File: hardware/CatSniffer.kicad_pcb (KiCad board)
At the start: 4 copper layers, 81 x 20 mm, 86 parts, among them J1 Antenna, J2 Conn_01x06_Female, J3 Conn_01x06_Female, P1 USB_C_Plug_USB2.0, SW1 SW, U1 AP2112K-3.3, U2 RFSW8006QTR7, U3 ATSAMD21E18A, U4 0900PC15A0036, U5 0900FM15D0039, U6 SW409, U7 SX1262IMLTRT, U8 CC1352R1F3RGZR, Y1 48MHz, Y2 32.768kHz, Y3 32Mhz

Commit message: ChngCC1352P
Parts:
- U8: value CC1352R1F3RGZR -> CC1352P1F3RGZT
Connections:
- U8 pad 5: /RX_TX -> Net-(U8-Pad5)
- U8 pad 6: Net-(C34-Pad1) -> Net-(U8-Pad6)
- U8 pad 7: Net-(C36-Pad1) -> /RX_TX
- U8 pad 8: Net-(U8-Pad8) -> Net-(C34-Pad1)
- U8 pad 9: Net-(U8-Pad9) -> Net-(C36-Pad1)
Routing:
- net Net-(C36-Pad1): track 4.32 -> 3.40 mm
- net /RX_TX: track 6.78 -> 7.66 mm
- net Net-(C34-Pad1): track 6.01 -> 5.45 mm

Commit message: UpdateKicad6
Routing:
- added copper zone on In2.Cu, net +3V3
- added copper zone on In2.Cu, net /VDDR
- added copper zone on In2.Cu, net /VDDS
- added copper zone on In1.Cu, net GND
- removed copper zone on VCC, net +3V3
- removed copper zone on VCC, net /VDDR
- removed copper zone on VCC, net /VDDS
- removed copper zone on GND, net GND
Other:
- net class Default removed

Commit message: update version
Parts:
- removed C28, C30: 47pF, Capacitor_SMD:C_0603_1608Metric
- U6: value SW409 -> PE42421; footprint CatSniffer:SW409 -> Package_TO_SOT_SMD:SOT-363_SC-70-6
- moved R8 0.59 mm to (139.1, 105.1)
- moved R7 0.38 mm to (139.0, 100.8)
- moved U6 0.20 mm to (138.9, 103.0), turned to 0 degrees
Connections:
- J2 pad 6: Net-(J2-Pad6) -> unconnected-(J2-Pad6)
- J3 pad 6: Net-(J3-Pad6) -> unconnected-(J3-Pad6)
- U1 pad 4: Net-(U1-Pad4) -> unconnected-(U1-Pad4)
- U6 pad 1: Net-(C28-Pad2) -> /SW_RFO
- U6 pad 3: Net-(C30-Pad2) -> /SW_RFI
- U8 pad 10: Net-(U8-Pad10) -> unconnected-(U8-Pad10)
- U8 pad 11: Net-(U8-Pad11) -> unconnected-(U8-Pad11)
- U8 pad 12: Net-(U8-Pad12) -> unconnected-(U8-Pad12)
- U8 pad 14: Net-(U8-Pad14) -> unconnected-(U8-Pad14)
- U8 pad 15: Net-(U8-Pad15) -> unconnected-(U8-Pad15)
- U8 pad 16: Net-(U8-Pad16) -> unconnected-(U8-Pad16)
- U8 pad 17: Net-(U8-Pad17) -> unconnected-(U8-Pad17)
- U8 pad 20: Net-(U8-Pad20) -> unconnected-(U8-Pad20)
- U8 pad 26: Net-(U8-Pad26) -> unconnected-(U8-Pad26)
- U8 pad 27: Net-(U8-Pad27) -> unconnected-(U8-Pad27)
- U8 pad 28: Net-(U8-Pad28) -> unconnected-(U8-Pad28)
- U8 pad 29: Net-(U8-Pad29) -> unconnected-(U8-Pad29)
- U8 pad 30: Net-(U8-Pad30) -> unconnected-(U8-Pad30)
- U8 pad 31: Net-(U8-Pad31) -> unconnected-(U8-Pad31)
- U8 pad 32: Net-(U8-Pad32) -> unconnected-(U8-Pad32)
- U8 pad 36: Net-(U8-Pad36) -> unconnected-(U8-Pad36)
- U8 pad 38: Net-(U8-Pad38) -> unconnected-(U8-Pad38)
- U8 pad 39: Net-(U8-Pad39) -> unconnected-(U8-Pad39)
- U8 pad 40: Net-(U8-Pad40) -> unconnected-(U8-Pad40)
- U8 pad 41: Net-(U8-Pad41) -> unconnected-(U8-Pad41)
- U8 pad 42: Net-(U8-Pad42) -> unconnected-(U8-Pad42)
- U8 pad 43: Net-(U8-Pad43) -> unconnected-(U8-Pad43)
- U8 pad 5: Net-(U8-Pad5) -> unconnected-(U8-Pad5)
- U8 pad 6: Net-(U8-Pad6) -> unconnected-(U8-Pad6)
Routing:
- net GND: track 309.6 -> 318.9 mm
- net /SW_RFI: track 2.87 -> 6.34 mm
- net /SW_RFO: track 3.97 -> 7.32 mm
- net Net-(C28-Pad2): track 2.47 -> 0.00 mm
- net Net-(C30-Pad2): track 2.45 -> 0.00 mm
- net Net-(C35-Pad1): track 4.70 -> 3.54 mm
- net /ANT_SW: track 36.8 -> 37.6 mm
- net Net-(C31-Pad1): track 2.77 -> 3.48 mm
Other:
- board text added: "CatSniffer V2.0"
- board text removed: "CatSniffer V1.2"

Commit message: Update label 2.0
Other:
- board text added: "CatSniffer v2.0"
- board text removed: "CatSniffer v1.2"
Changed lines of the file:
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@@
     (43 "Eco2.User" user "User.Eco2")
     (44 "Edge.Cuts" user)
-    (45 "Margin" user)
+    (45 "Margin" user "Margen")
     (46 "B.CrtYd" user "B.Courtyard")
     (47 "F.CrtYd" user "F.Courtyard")
@@
   (gr_line (start 90 120) (end 161 120) (layer "Edge.Cuts") (width 0.15))
   (gr_line (start 85 105) (end 85 115) (layer "Edge.Cuts") (width 0.15))
-  (gr_text "CatSniffer\nv1.2" (at 98.298 110.236) (layer "B.SilkS")
+  (gr_text "CatSniffer\nv2.0" (at 98.298 110.236) (layer "B.SilkS")
     (effects (font (size 1.5 1.5) (thickness 0.25)) (justify mirror))
   )

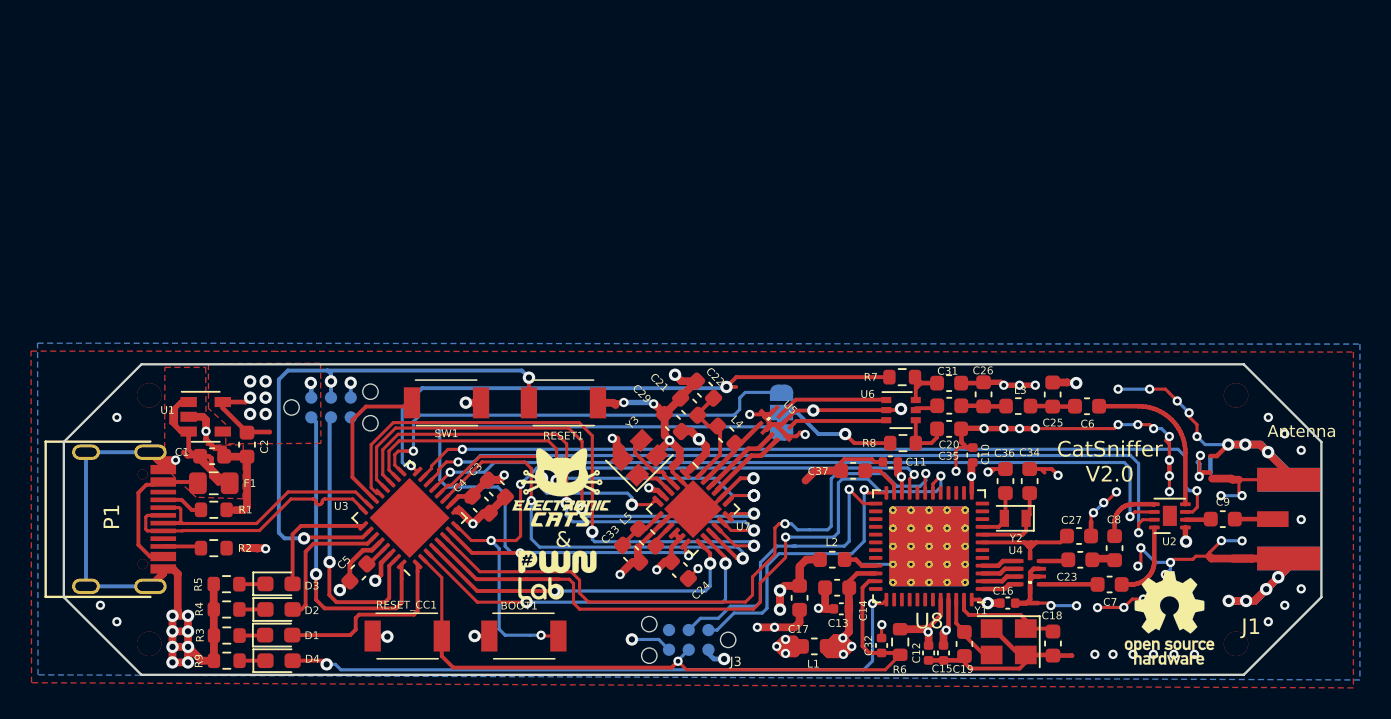
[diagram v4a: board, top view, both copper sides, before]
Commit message: change of components rp2040
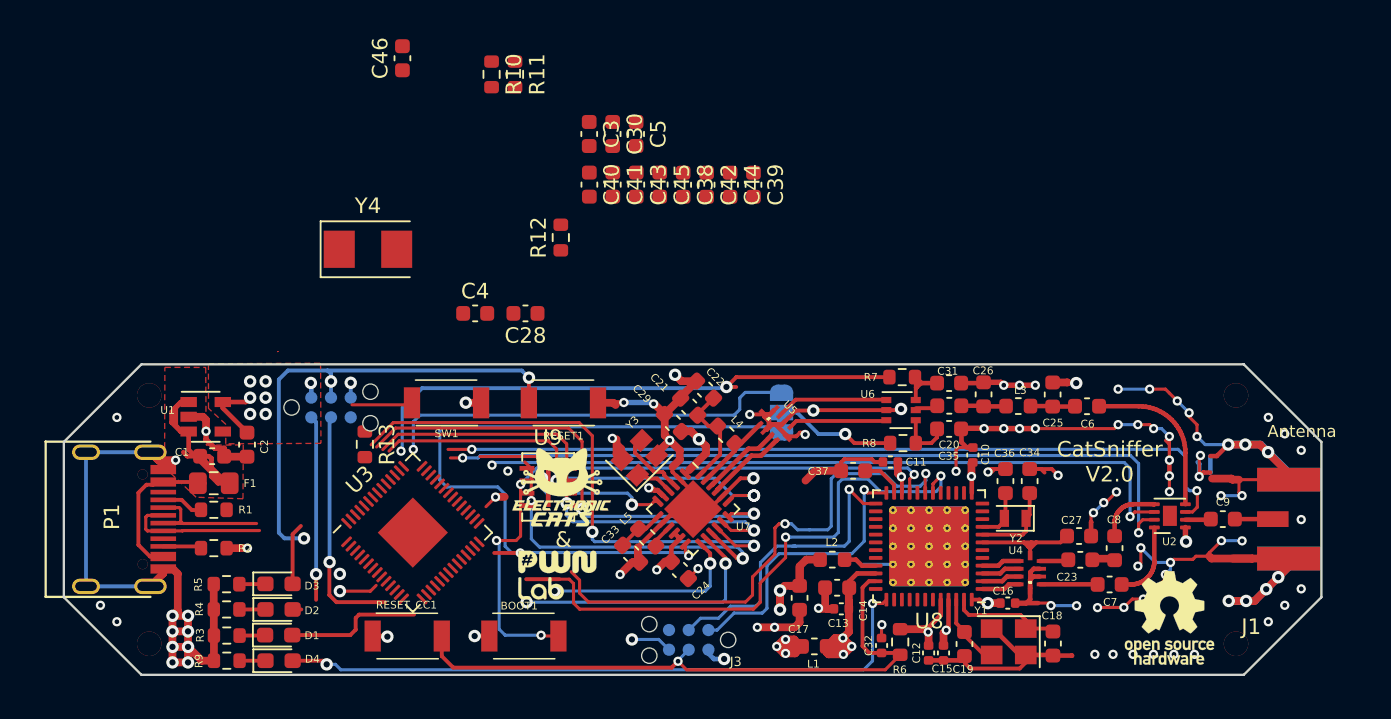
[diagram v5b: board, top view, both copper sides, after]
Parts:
- added C28: 27pF, Capacitor_SMD:C_0603_1608Metric, F.Cu at (114.7, 96.7)
- added C30: 0.1uF, Capacitor_SMD:C_0603_1608Metric, F.Cu at (120.3, 85.2)
- added C38: 1uF, Capacitor_SMD:C_0603_1608Metric, F.Cu at (124.9, 88.4)
- added C39: 0.1uF, Capacitor_SMD:C_0603_1608Metric, F.Cu at (129.4, 88.4)
- added C40: 0.1uF, Capacitor_SMD:C_0603_1608Metric, F.Cu at (118.8, 88.4)
- added C41: 0.1uF, Capacitor_SMD:C_0603_1608Metric, F.Cu at (120.4, 88.4)
- added C42: 0.1uF, Capacitor_SMD:C_0603_1608Metric, F.Cu at (126.4, 88.4)
- added C43: 0.1uF, Capacitor_SMD:C_0603_1608Metric, F.Cu at (121.9, 88.4)
- added C44: 0.1uF, Capacitor_SMD:C_0603_1608Metric, F.Cu at (127.9, 88.4)
- added C45: 0.1uF, Capacitor_SMD:C_0603_1608Metric, F.Cu at (123.4, 88.4)
- added C46: 0.1uF, Capacitor_SMD:C_0603_1608Metric, F.Cu at (106.8, 80.3)
- added R10: 27, Resistor_SMD:R_0603_1608Metric, F.Cu at (112.5, 81.3)
- added R11: 27, Resistor_SMD:R_0603_1608Metric, F.Cu at (114.1, 81.3)
- added R12: 1k, Resistor_SMD:R_0603_1608Metric, F.Cu at (117.0, 91.8)
- added R13: 10k, Resistor_SMD:R_0603_1608Metric, F.Cu at (104.4, 105.2)
- added U9: W25Q16JV, CatSniffer:W25Q16JVUUIQ, F.Cu at (116.2, 107.9)
- added Y4: 12MHz, Crystal:Crystal_SMD_5032-2Pin_5.0x3.2mm, F.Cu at (104.6, 92.6)
- C3: value 0.1uF -> 1uF
- C4: value 0.1uF -> 27pF
- U3: value ATSAMD21E18A -> RP2040; footprint Package_DFN_QFN:QFN-32-1EP_5x5mm_P0.5mm_EP3.65x3.65mm -> Package_DFN_QFN:QFN-56-1EP_7x7mm_P0.4mm_EP3.2x3.2mm
- moved C5 33.4 mm to (121.9, 85.2), turned to -90 degrees
- moved C3 23.6 mm to (118.8, 85.2), turned to -90 degrees
- moved C4 12.3 mm to (111.5, 96.7), turned to 0 degrees
- moved U3 0.97 mm to (107.5, 110.8), turned to 45 degrees
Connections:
- C3 pad 1: +3V3 -> +1V2
- C32 pad 1: /RESET_CC -> /RTS
- C4 pad 1: GND -> Net-(C4-Pad1)
- C4 pad 2: +3V3 -> GND
- C5 pad 1: GND -> +1V2
- C5 pad 2: Net-(C5-Pad2) -> GND
- J3 pad 3: /RESET_CC -> /RTS
- R6 pad 1: /RESET_CC -> /RTS
- RESET_CC1 pad 2: /RESET_CC -> /RTS
- SW1 pad 1: /U_SWITCH -> /QSPI_SS
- U3 pad 1: /LED3 -> +3V3
- U3 pad 10: GND -> +3V3
- U3 pad 11: /RESET_SX -> /CIPO
- U3 pad 12: /DIO3 -> /NSS
- U3 pad 14: /CTF2 -> /JTAG/TCK
- U3 pad 15: /CTF1 -> /cJTAG_TMSC
- U3 pad 16: /ANT_SW -> /JTAG/TDI
- U3 pad 17: /DIO22 -> /JTAG/TDO
- U3 pad 18: /NSS -> /RTS
- U3 pad 19: /COPI -> GND
- U3 pad 2: /RESET_CC -> /TXD
- U3 pad 20: /SCK -> Net-(C4-Pad1)
- U3 pad 21: /CIPO -> Net-(R12-Pad2)
- U3 pad 22: /U_SWITCH -> +3V3
- U3 pad 23: /D- -> +1V2
- U3 pad 24: /D+ -> /SWCLK
- U3 pad 25: /LED1 -> /SWDIO
- U3 pad 27: /LED2 -> /LED1
- U3 pad 28: GND -> /LED2
- U3 pad 29: Net-(C5-Pad2) -> /CTF2
- U3 pad 3: /BUSY -> /RXD
- U3 pad 30: +3V3 -> /CTF1
- U3 pad 31: /SWCLK -> /ANT_SW
- U3 pad 32: /SWDIO -> /DIO22
- U3 pad 33: (no net) -> +3V3
- U3 pad 4: /DIO1 -> /BOOT
- U3 pad 5: /TXD -> /RTS
- U3 pad 6: /RXD -> /BUSY
- U3 pad 7: /DIO2 -> /DIO1
- U3 pad 8: /BOOT -> /SCK
- U3 pad 9: +3V3 -> /COPI
- U8 pad 26: unconnected-(U8-Pad26) -> /JTAG/TDI
- U8 pad 27: unconnected-(U8-Pad27) -> /JTAG/TDO
- U8 pad 35: /RESET_CC -> /RTS
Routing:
- net /RESET_CC: track 46.8 -> 0.00 mm, vias 1 -> 0
- net /RTS: track 0.00 -> 41.3 mm, vias 0 -> 1
- net GND: track 318.9 -> 304.9 mm, vias 100 -> 98
- net /U_SWITCH: track 10.4 -> 0.00 mm
- net /RXD: track 42.6 -> 33.6 mm
- net /DIO1: track 22.0 -> 13.1 mm
- net /LED2: track 9.21 -> 0.66 mm
- net /D-: track 17.6 -> 9.16 mm
- net /SWDIO: track 20.6 -> 12.3 mm
- net /D+: track 17.6 -> 9.33 mm
- net +3V3: track 29.8 -> 22.0 mm, vias 16 -> 15
- net /BUSY: track 24.9 -> 17.3 mm
- net /TXD: track 46.3 -> 39.7 mm
- net /RESET_SX: track 28.3 -> 22.2 mm
- net /QSPI_SS: track 0.00 -> 4.68 mm
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- removed copper zone on B.Cu, net GND
- removed copper zone on F.Cu, net GND
- removed copper zone on In1.Cu, net GND

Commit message: change to rp2040
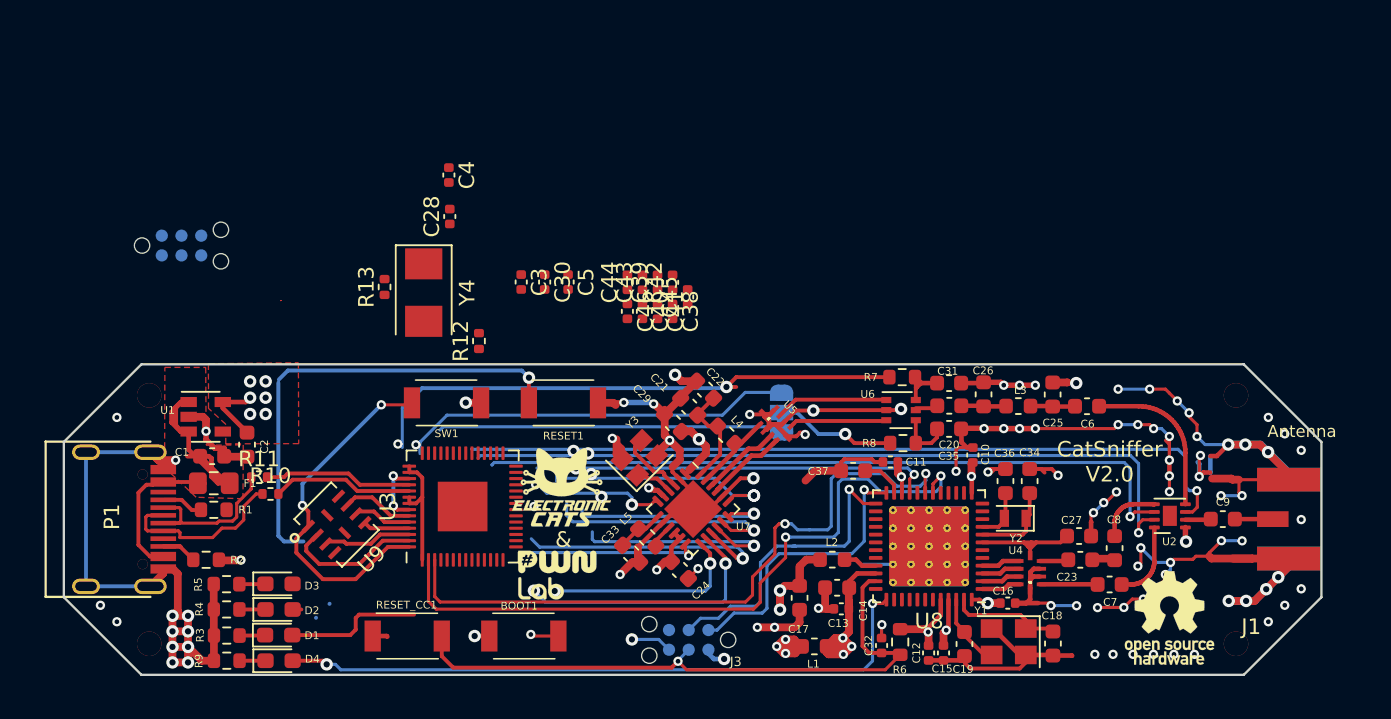
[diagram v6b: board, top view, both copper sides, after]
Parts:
- C28, C3, C30, C38, C39, C4, C40, C41, C42, C43, C44, C45, C46, C5: footprint Capacitor_SMD:C_0603_1608Metric -> Capacitor_SMD:C_0402_1005Metric
- R10, R11, R12, R13: footprint Resistor_SMD:R_0603_1608Metric -> Resistor_SMD:R_0402_1005Metric
- moved R11 30.7 mm to (97.6, 107.3), turned to 0 degrees
- moved R10 30.5 mm to (98.3, 108.3), turned to 0 degrees
- moved C46 21.8 mm to (121.3, 96.6), turned to -90 degrees
- moved J2 14.2 mm to (92.6, 92.3)
- moved U9 13.8 mm to (102.6, 110.3), turned to 45 degrees
- moved C3 10.5 mm to (114.5, 94.7)
- moved C30 10.5 mm to (116.0, 94.7)
- moved C5 10.5 mm to (117.5, 94.7)
- moved R13 10.2 mm to (105.7, 95.0), turned to 90 degrees
- moved C44 9.12 mm to (121.3, 94.7), turned to 90 degrees
- moved C4 9.07 mm to (109.8, 87.8), turned to -90 degrees
- moved C40 8.85 mm to (122.3, 96.6)
- moved C39 8.81 mm to (123.2, 94.7), turned to 90 degrees
- moved C41 8.66 mm to (123.2, 96.6)
- moved R12 8.50 mm to (111.7, 98.5)
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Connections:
- net /RTS renamed /RESET_CC
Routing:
- net /CIPO: track 35.3 -> 13.9 mm, vias 3 -> 1
- net /QSPI_SS: track 4.68 -> 23.7 mm, vias 0 -> 2
- net /SCK: track 31.8 -> 13.4 mm
- net /COPI: track 31.8 -> 15.5 mm
- net /SWCLK: track 15.4 -> 0.00 mm, vias 1 -> 0
- net /BOOT: track 42.1 -> 27.6 mm, vias 4 -> 2
- net /DIO2: track 47.8 -> 33.8 mm, vias 2 -> 1
- net /NSS: track 28.7 -> 15.4 mm
- net /SWDIO: track 12.3 -> 0.01 mm, vias 1 -> 0
- net /RXD: track 33.6 -> 43.6 mm
- net Net-(R11-Pad2): track 0.00 -> 9.56 mm
- net Net-(R10-Pad2): track 0.00 -> 9.11 mm
- net /QSPI_SD1: track 0.00 -> 8.94 mm
- net +3V3: track 22.0 -> 29.3 mm, vias 15 -> 13
- net /QSPI_SD2: track 0.00 -> 5.74 mm
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
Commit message: Initial routing
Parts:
- Y4: footprint Crystal:Crystal_SMD_5032-2Pin_5.0x3.2mm -> Crystal:Crystal_SMD_3225-4Pin_3.2x2.5mm
- moved C4 25.4 mm to (118.9, 111.5), turned to 0 degrees
- moved C40 24.5 mm to (105.0, 114.0)
- moved C41 24.5 mm to (106.0, 114.0)
- moved C38 24.1 mm to (107.4, 113.8), turned to 180 degrees
- moved C43 20.5 mm to (115.4, 114.0), turned to -90 degrees
- moved C5 20.2 mm to (100.4, 105.5), turned to 90 degrees
- moved C44 19.9 mm to (116.4, 114.0), turned to -90 degrees
- moved C45 19.2 mm to (115.4, 112.1)
- moved C42 19.1 mm to (116.4, 112.1)
- moved C28 18.6 mm to (118.3, 107.1), turned to 180 degrees
- moved C39 18.4 mm to (117.3, 112.1)
- moved C30 18.2 mm to (101.3, 105.5), turned to 90 degrees
- moved C46 17.9 mm to (117.3, 114.0)
- moved Y4 17.3 mm to (118.5, 109.3), turned to 0 degrees
- moved C3 16.3 mm to (102.3, 105.5), turned to 90 degrees
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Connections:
- U3 pad 14: /JTAG/TCK -> /cJTAG_TCK
- U3 pad 24: /SWCLK -> unconnected-(U3-Pad24)
- U3 pad 25: /SWDIO -> unconnected-(U3-Pad25)
- Y4 pad 2: Net-(C28-Pad1) -> GND
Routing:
- net GND: track 303.8 -> 359.9 mm, vias 96 -> 99
- net +3V3: track 29.3 -> 56.9 mm, vias 13 -> 17
- net /cJTAG_TMSC: track 18.8 -> 45.4 mm, vias 1 -> 3
- net /JTAG/TDO: track 0.00 -> 21.4 mm, vias 0 -> 1
- net +1V2: track 4.16 -> 20.2 mm, vias 2 -> 4
- net /COPI: track 15.5 -> 2.28 mm, vias 2 -> 1
- net /SCK: track 13.4 -> 26.1 mm
- net /BOOT: track 27.6 -> 36.5 mm, vias 2 -> 3
- net /LED3: track 8.83 -> 17.5 mm, vias 0 -> 2
- net /RESET: track 29.8 -> 38.0 mm
- net /DIO1: track 13.1 -> 20.8 mm
- net /BUSY: track 17.1 -> 23.2 mm
- net /DIO3: track 8.93 -> 15.0 mm, vias 3 -> 2
- net /RESET_CC: track 41.3 -> 47.2 mm
- net /ANT_SW: track 35.4 -> 29.7 mm
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
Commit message: routing rp2040
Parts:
- moved C42 16.9 mm to (100.2, 107.2), turned to 45 degrees
- moved C30 14.2 mm to (115.4, 107.6)
- moved C45 12.9 mm to (104.1, 106.0)
- moved C44 12.1 mm to (107.6, 105.6), turned to 180 degrees
- moved C43 9.87 mm to (105.5, 113.7), turned to 180 degrees
- moved C38 8.21 mm to (105.1, 106.0), turned to 90 degrees
- moved C40 8.11 mm to (106.1, 106.0), turned to 90 degrees
- moved R11 7.81 mm to (105.3, 108.4)
- moved R10 7.08 mm to (105.3, 109.4)
- moved C41 5.65 mm to (103.0, 109.2), turned to 135 degrees
- moved R13 5.33 mm to (99.3, 106.5), turned to -135 degrees
- moved C5 5.29 mm to (105.3, 107.4), turned to 180 degrees
- moved C46 4.57 mm to (116.5, 109.5), turned to 90 degrees
- moved R12 3.91 mm to (117.9, 109.9), turned to 0 degrees
- moved SW1 3.77 mm to (103.9, 102.5)
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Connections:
- J2 pad 1: +3V3 -> unconnected-(J2-Pad1)
- J2 pad 2: /SWDIO -> unconnected-(J2-Pad2)
- J2 pad 3: /RESET -> unconnected-(J2-Pad3)
- J2 pad 4: /SWCLK -> unconnected-(J2-Pad4)
- J2 pad 5: GND -> unconnected-(J2-Pad5)
- U3 pad 27: /LED1 -> unconnected-(U3-Pad27)
- U3 pad 28: /LED2 -> unconnected-(U3-Pad28)
- U3 pad 34: /U_SWITCH -> unconnected-(U3-Pad34)
- U3 pad 39: unconnected-(U3-Pad39) -> /LED2
- U3 pad 40: unconnected-(U3-Pad40) -> /LED1
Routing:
- net /JTAG/TDI: track 0.00 -> 27.1 mm, vias 0 -> 2
- net /RESET: track 38.0 -> 12.1 mm, vias 1 -> 2
- net GND: track 359.9 -> 382.7 mm, vias 99 -> 96
- net /LED2: track 0.66 -> 20.2 mm, vias 0 -> 2
- net /LED1: track 0.00 -> 17.6 mm, vias 0 -> 2
- net /CIPO: track 16.6 -> 2.85 mm
- net /RESET_SX: track 15.9 -> 2.67 mm
- net /DIO3: track 15.0 -> 2.26 mm, vias 2 -> 1
- net +3V3: track 56.9 -> 65.6 mm, vias 17 -> 15
- net Net-(R11-Pad2): track 9.56 -> 1.64 mm
- net /RESET_CC: track 47.2 -> 55.0 mm, vias 1 -> 3
- net Net-(R10-Pad2): track 9.11 -> 1.54 mm
- net /D-: track 11.0 -> 18.4 mm, vias 0 -> 2
- net /D+: track 11.6 -> 18.8 mm, vias 0 -> 2
- net /DIO2: track 30.1 -> 23.7 mm
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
